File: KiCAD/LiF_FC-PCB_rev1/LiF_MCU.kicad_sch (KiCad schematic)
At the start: 32 parts, among them J12 CAN Upstream, J40 ESP 3V3_{EN}, Q1 MMBT4401, Q2 MMBT4401, SW1 SW_Push, SW2 SW_Push, U6 ESP32-S3-WROOM-1, U7 CY7C65213-28PVXI

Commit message: Added MCU pinout, shanged shift registers to GPIO expanders to save pins on MCU
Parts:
- removed SW1, SW2: SW_Push, LiF_PCB_Footprints:SW_TL3301PF160QG, symbol Switch:SW_Push
- added J35, J41: ESP_DGB_CONN, Connector_PinHeader_1.27mm:PinHeader_1x14_P1.27mm_Vertical, symbol Connector:Conn_01x14_Socket
- added J42: ESP_DGB_CONN, Connector_PinHeader_1.27mm:PinHeader_1x12_P1.27mm_Vertical, symbol Connector:Conn_01x12_Socket
- added SW1: Flash, LiF_PCB_Footprints:SW_TL3301PF160QG, symbol LiF_PCB_Symbols:TL3301PF160QG
- added SW2: Reset, LiF_PCB_Footprints:SW_TL3301PF160QG, symbol LiF_PCB_Symbols:TL3301PF160QG
- added TP27: SCL, TestPoint:TestPoint_Loop_D1.80mm_Drill1.0mm_Beaded, symbol Connector:TestPoint
- added TP28: SDA, TestPoint:TestPoint_Loop_D1.80mm_Drill1.0mm_Beaded, symbol Connector:TestPoint
- added TP29: GND, TestPoint:TestPoint_Loop_D1.80mm_Drill1.0mm_Beaded, symbol Connector:TestPoint
- renumbered J40 to J12, J12 to J13, R61 to R25, R25 to R26, R26 to R27, R27 to R28, R28 to R29, R29 to R30, R30 to R31, R31 to R32, R32 to R33
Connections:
- net ACC_INT1: now also U6.8 (IO15), J35.8 (Pin_8)
- net ACC_INT2: now also U6.9 (IO16), J35.9 (Pin_9)
- net AMP_ENABLE: now also U6.31 (IO38), J41.5 (Pin_5)
- net CAN.RXD: now also U6.21 (IO13), J42.7 (Pin_7)
- net CAN.TXD: now also U6.22 (IO14), J42.8 (Pin_8)
- net CHIP_PU: now also J35.3 (Pin_3), SW2.1, SW2.2
- net ENC.A: now also U6.18 (IO10), J42.4 (Pin_4)
- net ENC.B: now also U6.19 (IO11), J42.5 (Pin_5)
- net ENC.SW: now also U6.20 (IO12), J42.6 (Pin_6)
- net ESP_3V3: now also R23.2, R24.2, J35.2 (Pin_2)
- net GND: now also J35.1 (Pin_1), J41.14 (Pin_14), SW1.3, SW1.4, SW2.3, SW2.4, TP29.1
- net Load Cell: now also U6.39 (IO1), J41.13 (Pin_13)
- net ESP32_10: now reaches U6.10 (IO17)
- net ESP32_10: now also J35.10 (Pin_10)
- net ESP32_11: now reaches U6.11 (IO18)
- net ESP32_11: now also J35.11 (Pin_11)
- net ESP32_12: now reaches U6.12 (IO8)
- net ESP32_12: now also R23.1, R24.1, J35.12 (Pin_12), TP28.1
- net ESP32_13: now reaches U6.13 (USB_D-)
- net ESP32_13: now also J35.13 (Pin_13)
- net ESP32_14: now reaches U6.14 (USB_D+)
- net ESP32_14: now also J35.14 (Pin_14)
- net ESP32_15: now reaches U6.15 (IO3)
- net ESP32_15: now also J42.1 (Pin_1)
- net ESP32_16: now reaches U6.16 (IO46)
- net ESP32_16: now also J42.2 (Pin_2)
- net ESP32_17: now reaches U6.17 (IO9)
- net ESP32_17: now also J42.3 (Pin_3), TP27.1
- net ESP32_23: now reaches U6.23 (IO21)
- net ESP32_23: now also J42.9 (Pin_9)
- net ESP32_24: now reaches U6.24 (IO47)
- net ESP32_24: now also J42.10 (Pin_10)
- net ESP32_25: now reaches U6.25 (IO48)
- net ESP32_25: now also J42.11 (Pin_11)
- net ESP32_26: now reaches U6.26 (IO45)
- net ESP32_26: now also J42.12 (Pin_12)
- net ESP32_28: now reaches U6.28 (IO35)
- net ESP32_28: now also J41.2 (Pin_2)
- net ESP32_29: now reaches U6.29 (IO36)
- net ESP32_29: now also J41.3 (Pin_3)
- net ESP32_30: now reaches U6.30 (IO37)
- net ESP32_30: now also J41.4 (Pin_4)
- net ESP32_32: now reaches U6.32 (IO39)
- net ESP32_32: now also J41.6 (Pin_6)
- net ESP32_33: now reaches U6.33 (IO40)
- net ESP32_33: now also J41.7 (Pin_7)
- net ESP32_34: now reaches U6.34 (IO41)
- net ESP32_34: now also J41.8 (Pin_8)
- net ESP32_35: now reaches U6.35 (IO42)
- net ESP32_35: now also J41.9 (Pin_9)
- net ~{BTN_IRQ}: now reaches U6.38 (IO2)
- net ~{BTN_IRQ}: now also J41.12 (Pin_12)
- net ESP32_4: now reaches U6.4 (IO4)
- net ESP32_4: now also J35.4 (Pin_4)
- net ESP32_5: now reaches U6.5 (IO5)
- net ESP32_5: now also J35.5 (Pin_5)
- net ESP32_6: now reaches U6.6 (IO6)
- net ESP32_6: now also J35.6 (Pin_6)
- net ESP32_7: now reaches U6.7 (IO7)
- net ESP32_7: now also J35.7 (Pin_7)
- net ESP_RX renamed ESP32_37
- net ESP32_37: now also J41.11 (Pin_11)
- net ESP_TX renamed ESP32_36
- net ESP32_36: now also J41.10 (Pin_10)
- net GPIO0 renamed ESP32_27
- net ESP32_27: now also J41.1 (Pin_1), SW1.1, SW1.2
- no-connect marks 50 -> 13
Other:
- note added: "DEBUG CONNECTOR"
- note added: "ESP32-S3 Pin Assignment"
- note added: "External Connections"
- note added: "I2C DBG"
- note added: "JTAG interface"
- note added: "PSRAM"
- note added: "Power Input"
- note added: "Programming USB"
- note added: "Reset and Flash Buttons"
- note added: "free to use"
- note added: "strapping pin"
- note removed: "Reset and Program Buttons"
- title: (none) -> Lithium Firefly Custom FC/CC PCB
- moved on the sheet: C18, C19, C20, C21, C23, D10, F2, J12, Q1, Q2, R23, R24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

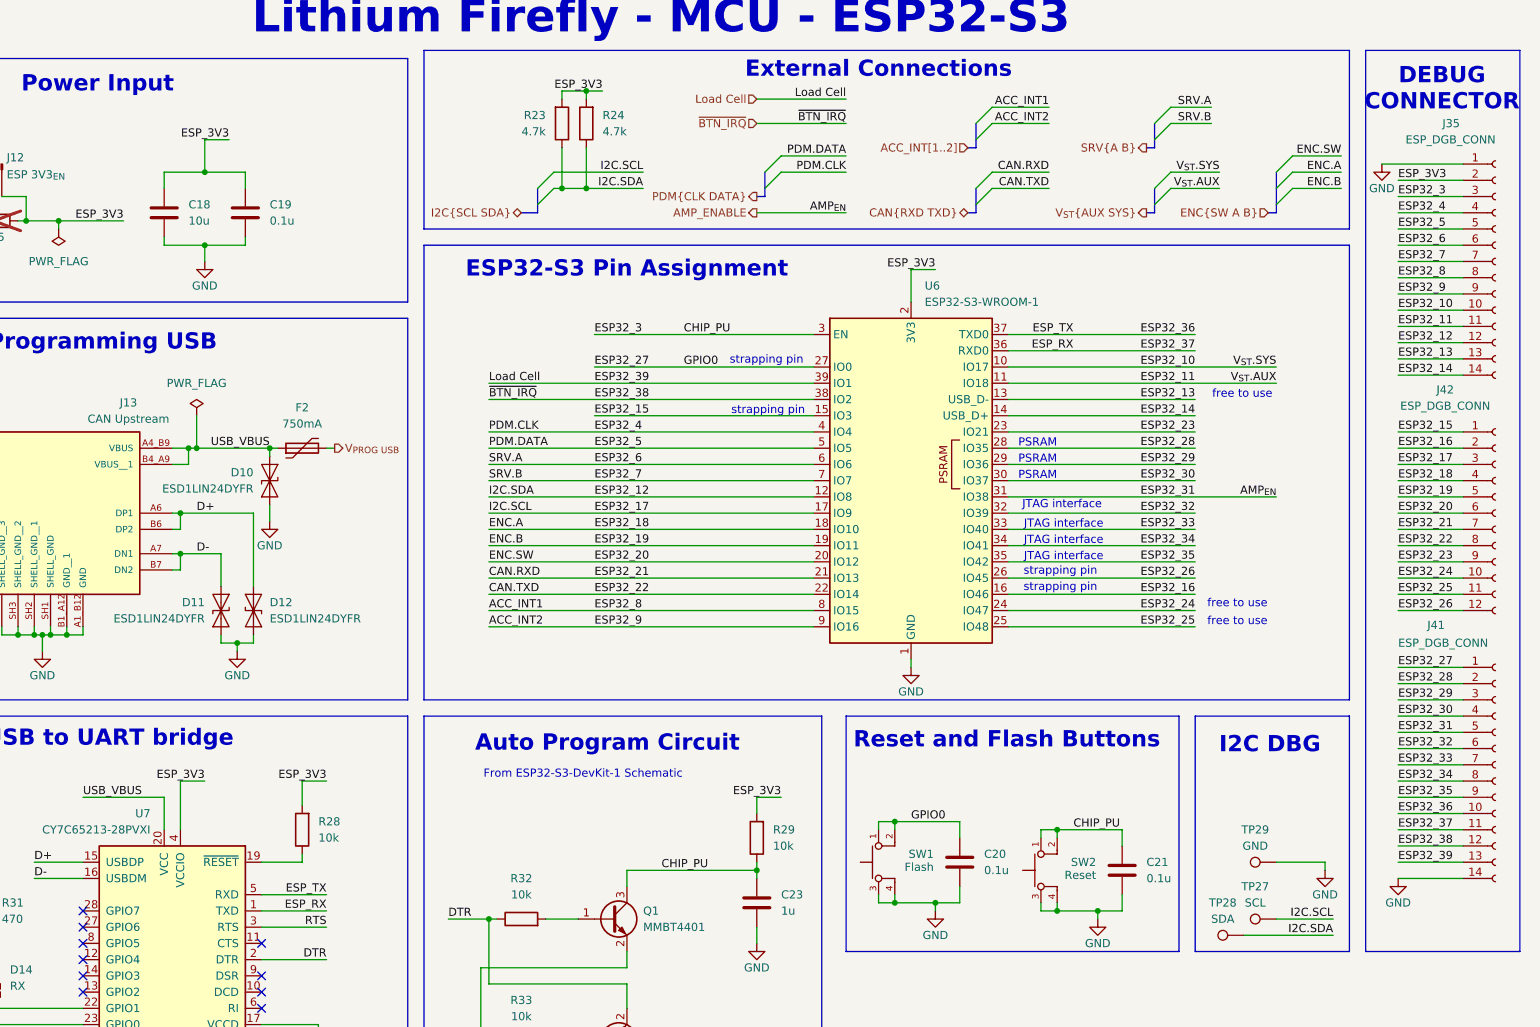
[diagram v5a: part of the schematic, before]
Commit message: Finalized schematic diagram. Only needs formatting fixes and resistor component sourcing info
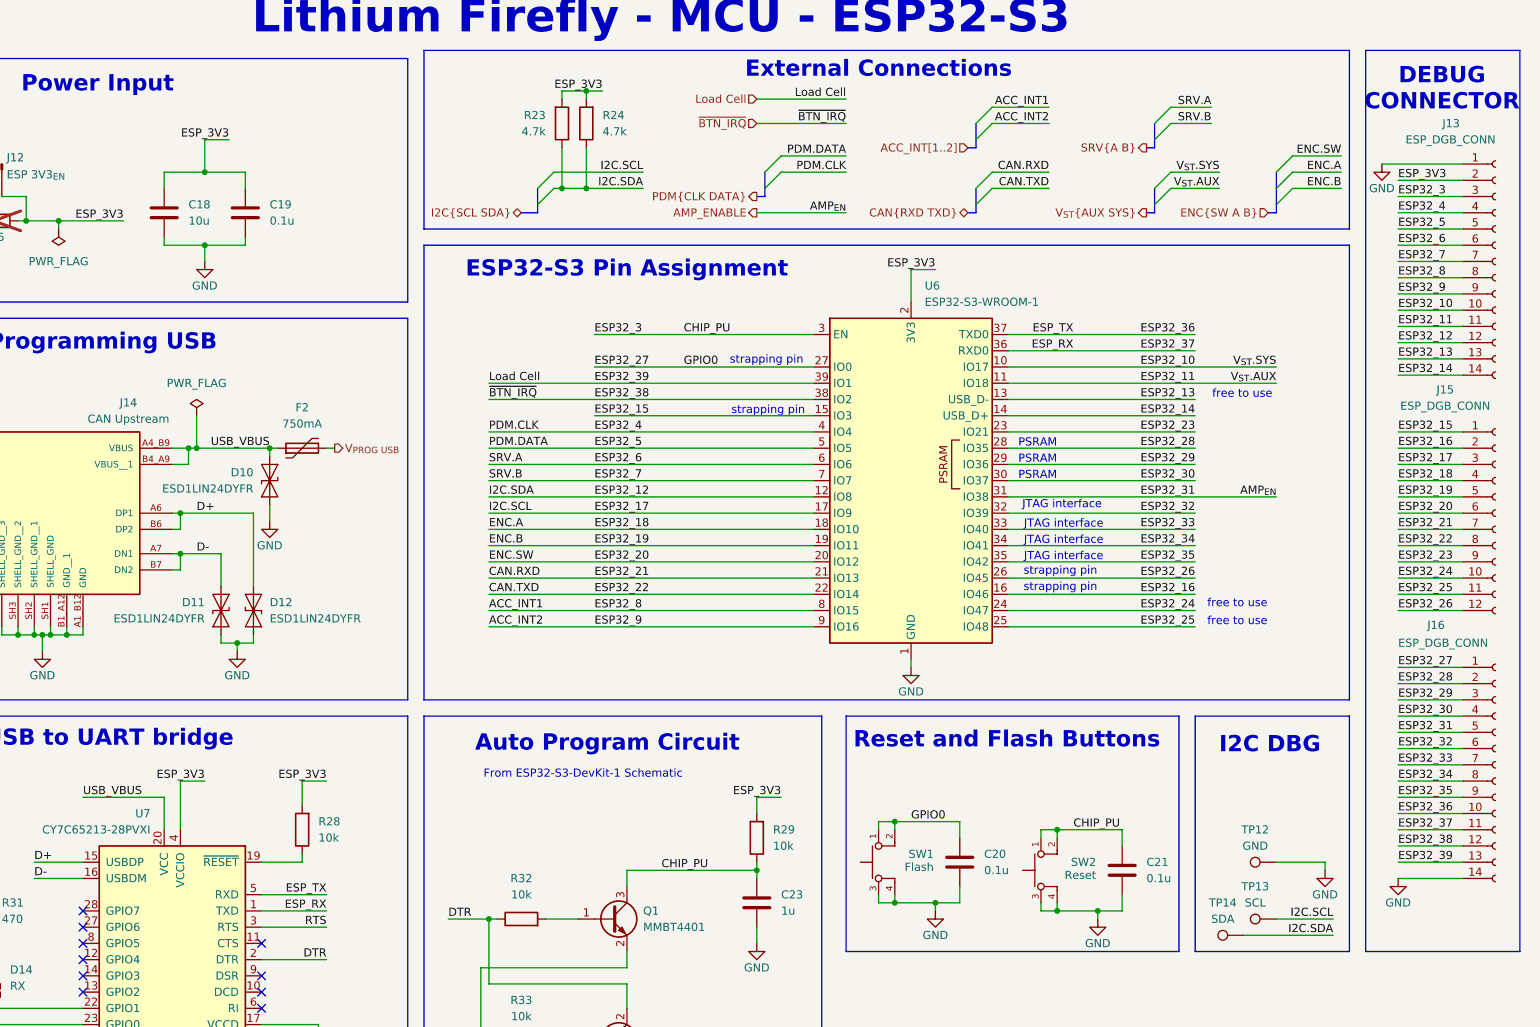
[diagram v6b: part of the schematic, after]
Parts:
- renumbered J35 to J13, J13 to J14, J42 to J15, J41 to J16, TP29 to TP12, TP27 to TP13, TP28 to TP14
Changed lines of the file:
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@@
 		(dnp no)
 		(fields_autoplaced yes)
-		(property "Reference" "TP28"
+		(property "Reference" "TP14"
 			(at 235.458 156.21 90)
 			(effects
@@
 			(project "LiF_FC-PCB_rev1"
 				(path "/9e3e8da7-e506-46c9-90e5-307e4ad30d29/fa6eb845-b5e3-4a8e-9c24-c1b567f4e987"
-					(reference "TP28")
+					(reference "TP14")
 					(unit 1)
 				)
@@
 		(on_board yes)
 		(dnp no)
-		(property "Reference" "#PWR040"
+		(property "Reference" "#PWR042"
 			(at 20.32 165.1 0)
 			(effects
@@
 			(project "LiF_FC-PCB_rev1"
 				(path "/9e3e8da7-e506-46c9-90e5-307e4ad30d29/fa6eb845-b5e3-4a8e-9c24-c1b567f4e987"
-					(reference "#PWR040")
+					(reference "#PWR042")
 					(unit 1)
 				)
@@
 		(on_board yes)
 		(dnp no)
-		(property "Reference" "#PWR0107"
+		(property "Reference" "#PWR040"
 			(at 262.89 158.75 0)
 			(effects
@@
 			(project "LiF_FC-PCB_rev1"
 				(path "/9e3e8da7-e506-46c9-90e5-307e4ad30d29/fa6eb845-b5e3-4a8e-9c24-c1b567f4e987"
-					(reference "#PWR0107")
+					(reference "#PWR040")
 					(unit 1)
 				)
@@
 		(on_board yes)
 		(dnp no)
-		(property "Reference" "J42"
+		(property "Reference" "J15"
 			(at 270.256 75.946 0)
 			(effects
@@
 			(project ""
 				(path "/9e3e8da7-e506-46c9-90e5-307e4ad30d29/fa6eb845-b5e3-4a8e-9c24-c1b567f4e987"
-					(reference "J42")
+					(reference "J15")
 					(unit 1)
 				)
@@
 		(on_board yes)
 		(dnp no)
-		(property "Reference" "#PWR033"
+		(property "Reference" "#PWR034"
 			(at 86.36 102.87 0)
 			(effects
@@
 			(project "LiF_FC-PCB_rev1"
 				(path "/9e3e8da7-e506-46c9-90e5-307e4ad30d29/fa6eb845-b5e3-4a8e-9c24-c1b567f4e987"
-					(reference "#PWR033")
+					(reference "#PWR034")
 					(unit 1)
 				)
@@
 		(on_board yes)
 		(dnp no)
-		(property "Reference" "J41"
+		(property "Reference" "J16"
 			(at 267.462 112.776 0)
 			(effects
@@
 			(project "LiF_FC-PCB_rev1"
 				(path "/9e3e8da7-e506-46c9-90e5-307e4ad30d29/fa6eb845-b5e3-4a8e-9c24-c1b567f4e987"
-					(reference "J41")
+					(reference "J16")
 					(unit 1)
 				)
@@
 		(on_board yes)
 		(dnp no)
-		(property "Reference" "J13"
+		(property "Reference" "J14"
 			(at 64.262 77.978 0)
 			(effects
@@
 			(project "LiF_FC-PCB_rev1"
 				(path "/9e3e8da7-e506-46c9-90e5-307e4ad30d29/fa6eb845-b5e3-4a8e-9c24-c1b567f4e987"
-					(reference "J13")
+					(reference "J14")
 					(unit 1)
 				)
@@
 		(dnp no)
 		(fields_autoplaced yes)
-		(property "Reference" "TP27"
+		(property "Reference" "TP13"
 			(at 240.538 153.67 90)
 			(effects
@@
 			(project "LiF_FC-PCB_rev1"
 				(path "/9e3e8da7-e506-46c9-90e5-307e4ad30d29/fa6eb845-b5e3-4a8e-9c24-c1b567f4e987"
-					(reference "TP27")
+					(reference "TP13")
 					(unit 1)
 				)
@@
 		(on_board yes)
 		(dnp no)
-		(property "Reference" "#PWR034"
+		(property "Reference" "#PWR038"
 			(at 186.69 125.73 0)
 			(effects
@@
 			(project "LiF_FC-PCB_rev1"
 				(path "/9e3e8da7-e506-46c9-90e5-307e4ad30d29/fa6eb845-b5e3-4a8e-9c24-c1b567f4e987"
-					(reference "#PWR034")
+					(reference "#PWR038")
 					(unit 1)
 				)
@@
 		(on_board yes)
 		(dnp no)
-		(property "Reference" "#PWR0108"
+		(property "Reference" "#PWR039"
 			(at 251.46 157.48 0)
 			(effects
@@
 			(project "LiF_FC-PCB_rev1"
 				(path "/9e3e8da7-e506-46c9-90e5-307e4ad30d29/fa6eb845-b5e3-4a8e-9c24-c1b567f4e987"
-					(reference "#PWR0108")
+					(reference "#PWR039")
 					(unit 1)
 				)
@@
 		(dnp no)
 		(fields_autoplaced yes)
-		(property "Reference" "TP29"
+		(property "Reference" "TP12"
 			(at 240.538 144.78 90)
 			(effects
@@
 			(project "LiF_FC-PCB_rev1"
 				(path "/9e3e8da7-e506-46c9-90e5-307e4ad30d29/fa6eb845-b5e3-4a8e-9c24-c1b567f4e987"
-					(reference "TP29")
+					(reference "TP12")
 					(unit 1)
 				)
@@
 		(on_board yes)
 		(dnp no)
-		(property "Reference" "#PWR041"
+		(property "Reference" "#PWR044"
 			(at 162.56 168.91 0)
 			(effects
@@
 			(project "LiF_FC-PCB_rev1"
 				(path "/9e3e8da7-e506-46c9-90e5-307e4ad30d29/fa6eb845-b5e3-4a8e-9c24-c1b567f4e987"
-					(reference "#PWR041")
+					(reference "#PWR044")
 					(unit 1)
 				)
@@
 		(on_board yes)
 		(dnp no)
-		(property "Reference" "J35"
+		(property "Reference" "J13"
 			(at 272.542 34.29 0)
 			(effects
@@
 			(project ""
 				(path "/9e3e8da7-e506-46c9-90e5-307e4ad30d29/fa6eb845-b5e3-4a8e-9c24-c1b567f4e987"
-					(reference "J35")
+					(reference "J13")
 					(unit 1)
 				)
@@
 		(on_board yes)
 		(dnp no)
-		(property "Reference" "#PWR039"
+		(property "Reference" "#PWR043"
 			(at 215.9 165.1 0)
 			(effects
@@
 			(project "LiF_FC-PCB_rev1"
 				(path "/9e3e8da7-e506-46c9-90e5-307e4ad30d29/fa6eb845-b5e3-4a8e-9c24-c1b567f4e987"
-					(reference "#PWR039")
+					(reference "#PWR043")
 					(unit 1)
 				)
@@
 		(on_board yes)
 		(dnp no)
-		(property "Reference" "#PWR0106"
+		(property "Reference" "#PWR032"
 			(at 260.35 46.99 0)
 			(effects
@@
 			(project "LiF_FC-PCB_rev1"
 				(path "/9e3e8da7-e506-46c9-90e5-307e4ad30d29/fa6eb845-b5e3-4a8e-9c24-c1b567f4e987"
-					(reference "#PWR0106")
+					(reference "#PWR032")
 					(unit 1)
 				)
@@
 		(on_board yes)
 		(dnp no)
-		(property "Reference" "#PWR043"
+		(property "Reference" "#PWR046"
 			(at 93.98 194.31 0)
 			(effects
@@
 			(project "LiF_FC-PCB_rev1"
 				(path "/9e3e8da7-e506-46c9-90e5-307e4ad30d29/fa6eb845-b5e3-4a8e-9c24-c1b567f4e987"
-					(reference "#PWR043")
+					(reference "#PWR046")
 					(unit 1)
 				)
@@
 		(on_board yes)
 		(dnp no)
-		(property "Reference" "#PWR042"
+		(property "Reference" "#PWR045"
 			(at 67.31 194.31 0)
 			(effects
@@
 			(project "LiF_FC-PCB_rev1"
 				(path "/9e3e8da7-e506-46c9-90e5-307e4ad30d29/fa6eb845-b5e3-4a8e-9c24-c1b567f4e987"
-					(reference "#PWR042")
+					(reference "#PWR045")
 					(unit 1)
 				)
@@
 		(on_board yes)
 		(dnp no)
-		(property "Reference" "#PWR032"
+		(property "Reference" "#PWR033"
 			(at 76.2 62.23 0)
 			(effects
@@
 			(project "LiF_FC-PCB_rev1"
 				(path "/9e3e8da7-e506-46c9-90e5-307e4ad30d29/fa6eb845-b5e3-4a8e-9c24-c1b567f4e987"
-					(reference "#PWR032")
+					(reference "#PWR033")
 					(unit 1)
 				)
@@
 		(on_board yes)
 		(dnp no)
-		(property "Reference" "#PWR038"
+		(property "Reference" "#PWR041"
 			(at 190.5 163.83 0)
 			(effects
@@
 			(project "LiF_FC-PCB_rev1"
 				(path "/9e3e8da7-e506-46c9-90e5-307e4ad30d29/fa6eb845-b5e3-4a8e-9c24-c1b567f4e987"
-					(reference "#PWR038")
+					(reference "#PWR041")
 					(unit 1)
 				)
